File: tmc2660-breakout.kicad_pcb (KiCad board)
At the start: 2 copper layers, 26.9 x 31.1 mm, 18 parts, among them P1 SPI, P2 StepDir, P3 Motor, P4 VCC, P5 VMOT, U1 TMC2660

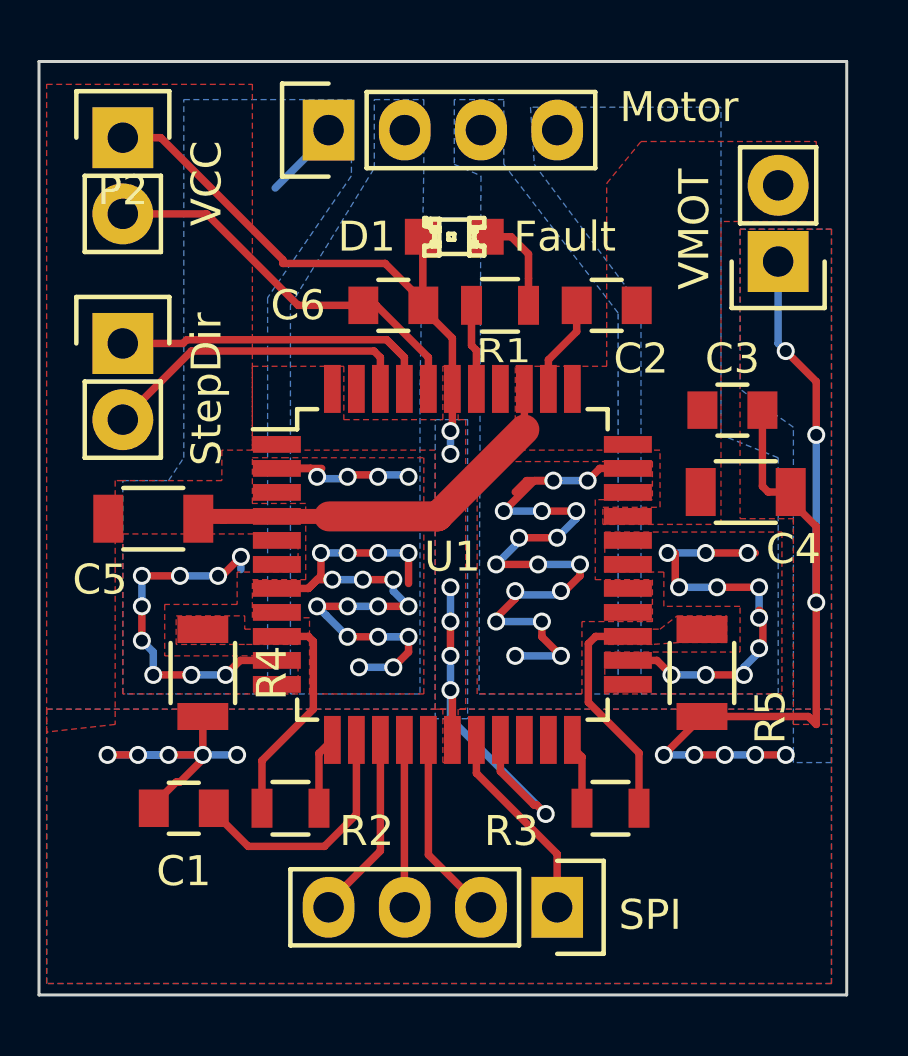
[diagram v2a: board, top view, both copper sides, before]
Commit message: o Add makefile to create fab files.
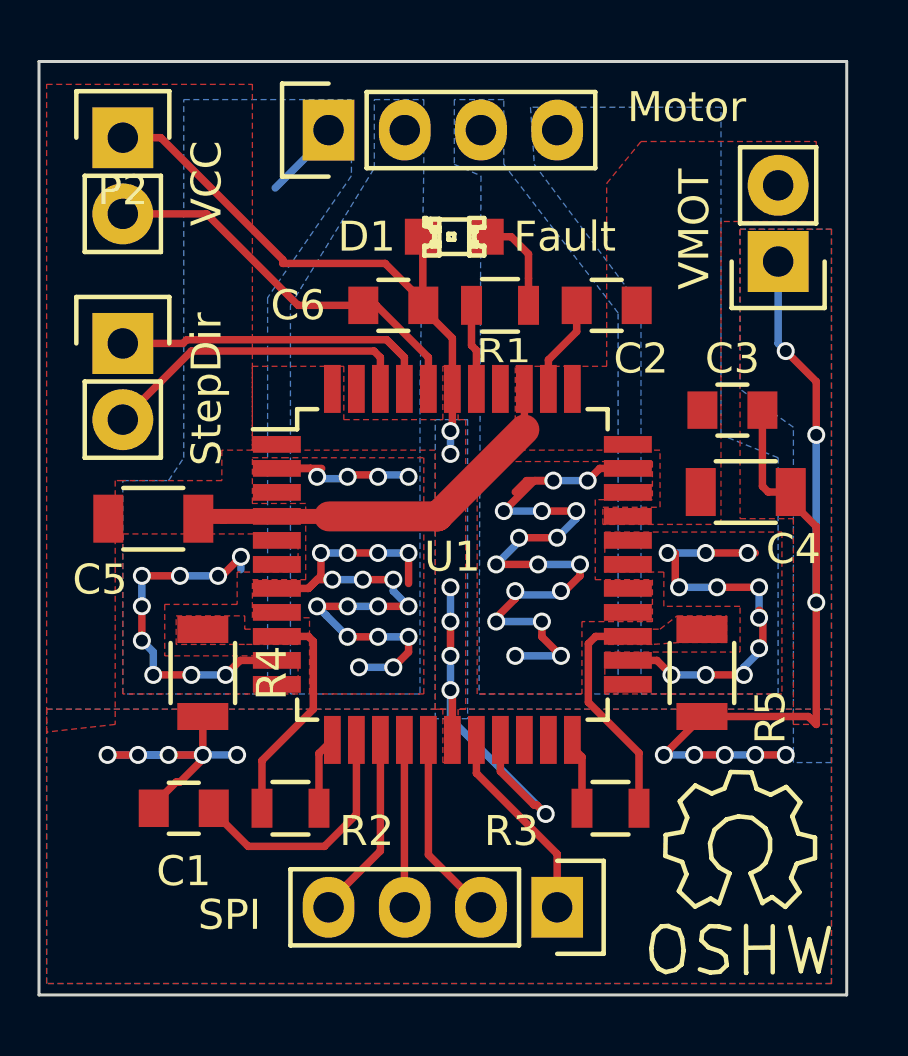
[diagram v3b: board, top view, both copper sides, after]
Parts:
- added REF**: Symbol_OSHW-Logo_SilkScreen, Symbols:Symbol_OSHW-Logo_SilkScreen, F.Cu at (139.4, 63.8)
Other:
- board text added: "%%gitversion%%"
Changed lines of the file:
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@@
 (kicad_pcb (version 4) (host pcbnew "(2015-12-17 BZR 6382, Git 22fdfa6)-product")
   (general
-    (links 56)
+    (links 0)
     (no_connects 0)
     (area 116.027999 37.541999 143.052001 68.757001)
     (thickness 1.6)
-    (drawings 5)
+    (drawings 6)
     (tracks 286)
     (zones 0)
-    (modules 18)
+    (modules 19)
     (nets 22)
   )
   (page A4)
   (layers
-    (0 F.Cu signal hide)
-    (31 B.Cu signal hide)
+    (0 F.Cu signal)
+    (31 B.Cu signal)
     (32 B.Adhes user)
     (33 F.Adhes user)
@@
       (effects (font (size 1 1) (thickness 0.15)))
     )
-    (fp_text value SPI (at 0.254 -3.1 360) (layer F.SilkS)
+    (fp_text value SPI (at 0.254 10.922 360) (layer F.SilkS)
       (effects (font (size 1 1) (thickness 0.15)))
     )
@@
       (effects (font (size 1 1) (thickness 0.15)))
     )
-    (fp_text value Motor (at 0.762 11.684 180) (layer F.SilkS)
+    (fp_text value Motor (at 0.762 11.938 180) (layer F.SilkS)
       (effects (font (size 1 1) (thickness 0.15)))
     )
@@
     )
   )
+  (module Symbols:Symbol_OSHW-Logo_SilkScreen locked (layer F.Cu)
+    (at 139.446 63.754)
+    (descr "Symbol, OSHW-Logo, Silk Screen,")
+    (tags "Symbol, OSHW-Logo, Silk Screen,")
+    (fp_text reference REF** (at 0.09906 -4.38912) (layer F.SilkS) hide
+      (effects (font (size 1 1) (thickness 0.15)))
+    )
+    (fp_text value Symbol_OSHW-Logo_SilkScreen (at 0.30988 6.56082) (layer F.Fab)
+      (effects (font (size 1 1) (thickness 0.15)))
+    )
+    (fp_line (start 1.66878 2.68986) (end 2.02946 4.16052) (layer F.SilkS) (width 0.15))
+    (fp_line (start 2.02946 4.16052) (end 2.30886 3.0988) (layer F.SilkS) (width 0.15))
+    (fp_line (start 2.30886 3.0988) (end 2.61874 4.17068) (layer F.SilkS) (width 0.15))
+    (fp_line (start 2.61874 4.17068) (end 2.9591 2.72034) (layer F.SilkS) (width 0.15))
+    (fp_line (start 0.24892 3.38074) (end 1.03886 3.37058) (layer F.SilkS) (width 0.15))
+    (fp_line (start 1.03886 3.37058) (end 1.04902 3.38074) (layer F.SilkS) (width 0.15))
+    (fp_line (start 1.04902 3.38074) (end 1.04902 3.37058) (layer F.SilkS) (width 0.15))
+    (fp_line (start 1.08966 2.65938) (end 1.08966 4.20116) (layer F.SilkS) (width 0.15))
+    (fp_line (start 0.20066 2.64922) (end 0.20066 4.21894) (layer F.SilkS) (width 0.15))
+    (fp_line (start 0.20066 4.21894) (end 0.21082 4.20878) (layer F.SilkS) (width 0.15))
+    (fp_line (start -0.35052 2.75082) (end -0.70104 2.66954) (layer F.SilkS) (width 0.15))
+    (fp_line (start -0.70104 2.66954) (end -1.02108 2.65938) (layer F.SilkS) (width 0.15))
+    (fp_line (start -1.02108 2.65938) (end -1.25984 2.86004) (layer F.SilkS) (width 0.15))
+    (fp_line (start -1.25984 2.86004) (end -1.29032 3.12928) (layer F.SilkS) (width 0.15))
+    (fp_line (start -1.29032 3.12928) (end -1.04902 3.37058) (layer F.SilkS) (width 0.15))
+    (fp_line (start -1.04902 3.37058) (end -0.6604 3.50012) (layer F.SilkS) (width 0.15))
+    (fp_line (start -0.6604 3.50012) (end -0.48006 3.66014) (layer F.SilkS) (width 0.15))
+    (fp_line (start -0.48006 3.66014) (end -0.43942 3.95986) (layer F.SilkS) (width 0.15))
+    (fp_line (start -0.43942 3.95986) (end -0.67056 4.18084) (layer F.SilkS) (width 0.15))
+    (fp_line (start -0.67056 4.18084) (end -0.9906 4.20878) (layer F.SilkS) (width 0.15))
+    (fp_line (start -0.9906 4.20878) (end -1.34112 4.09956) (layer F.SilkS) (width 0.15))
+    (fp_line (start -2.37998 2.64922) (end -2.6289 2.66954) (layer F.SilkS) (width 0.15))
+    (fp_line (start -2.6289 2.66954) (end -2.8702 2.91084) (layer F.SilkS) (width 0.15))
+    (fp_line (start -2.8702 2.91084) (end -2.9591 3.40106) (layer F.SilkS) (width 0.15))
+    (fp_line (start -2.9591 3.40106) (end -2.93116 3.74904) (layer F.SilkS) (width 0.15))
+    (fp_line (start -2.93116 3.74904) (end -2.7305 4.06908) (layer F.SilkS) (width 0.15))
+    (fp_line (start -2.7305 4.06908) (end -2.47904 4.191) (layer F.SilkS) (width 0.15))
+    (fp_line (start -2.47904 4.191) (end -2.16916 4.11988) (layer F.SilkS) (width 0.15))
+    (fp_line (start -2.16916 4.11988) (end -1.95072 3.93954) (layer F.SilkS) (width 0.15))
+    (fp_line (start -1.95072 3.93954) (end -1.8796 3.4798) (layer F.SilkS) (width 0.15))
+    (fp_line (start -1.8796 3.4798) (end -1.9304 3.07086) (layer F.SilkS) (width 0.15))
+    (fp_line (start -1.9304 3.07086) (end -2.03962 2.78892) (layer F.SilkS) (width 0.15))
+    (fp_line (start -2.03962 2.78892) (end -2.4003 2.65938) (layer F.SilkS) (width 0.15))
+    (fp_line (start -1.78054 0.92964) (end -2.03962 1.49098) (layer F.SilkS) (width 0.15))
+    (fp_line (start -2.03962 1.49098) (end -1.50114 2.00914) (layer F.SilkS) (width 0.15))
+    (fp_line (start -1.50114 2.00914) (end -0.98044 1.7399) (layer F.SilkS) (width 0.15))
+    (fp_line (start -0.98044 1.7399) (end -0.70104 1.89992) (layer F.SilkS) (width 0.15))
+    (fp_line (start 0.73914 1.8796) (end 1.06934 1.6891) (layer F.SilkS) (width 0.15))
+    (fp_line (start 1.06934 1.6891) (end 1.50876 2.0193) (layer F.SilkS) (width 0.15))
+    (fp_line (start 1.50876 2.0193) (end 1.9812 1.52908) (layer F.SilkS) (width 0.15))
+    (fp_line (start 1.9812 1.52908) (end 1.69926 1.04902) (layer F.SilkS) (width 0.15))
+    (fp_line (start 1.69926 1.04902) (end 1.88976 0.57912) (layer F.SilkS) (width 0.15))
+    (fp_line (start 1.88976 0.57912) (end 2.49936 0.39116) (layer F.SilkS) (width 0.15))
+    (fp_line (start 2.49936 0.39116) (end 2.49936 -0.28956) (layer F.SilkS) (width 0.15))
+    (fp_line (start 2.49936 -0.28956) (end 1.94056 -0.42926) (layer F.SilkS) (width 0.15))
+    (fp_line (start 1.94056 -0.42926) (end 1.7399 -1.00076) (layer F.SilkS) (width 0.15))
+    (fp_line (start 1.7399 -1.00076) (end 2.00914 -1.47066) (layer F.SilkS) (width 0.15))
+    (fp_line (start 2.00914 -1.47066) (end 1.53924 -1.9812) (layer F.SilkS) (width 0.15))
+    (fp_line (start 1.53924 -1.9812) (end 1.02108 -1.71958) (layer F.SilkS) (width 0.15))
+    (fp_line (start 1.02108 -1.71958) (end 0.55118 -1.92024) (layer F.SilkS) (width 0.15))
+    (fp_line (start 0.55118 -1.92024) (end 0.381 -2.46126) (layer F.SilkS) (width 0.15))
+    (fp_line (start 0.381 -2.46126) (end -0.30988 -2.47904) (layer F.SilkS) (width 0.15))
+    (fp_line (start -0.30988 -2.47904) (end -0.5207 -1.9304) (layer F.SilkS) (width 0.15))
+    (fp_line (start -0.5207 -1.9304) (end -0.9398 -1.76022) (layer F.SilkS) (width 0.15))
+    (fp_line (start -0.9398 -1.76022) (end -1.49098 -2.02946) (layer F.SilkS) (width 0.15))
+    (fp_line (start -1.49098 -2.02946) (end -2.00914 -1.50114) (layer F.SilkS) (width 0.15))
+    (fp_line (start -2.00914 -1.50114) (end -1.76022 -0.96012) (layer F.SilkS) (width 0.15))
+    (fp_line (start -1.76022 -0.96012) (end -1.9304 -0.48006) (layer F.SilkS) (width 0.15))
+    (fp_line (start -1.9304 -0.48006) (end -2.47904 -0.381) (layer F.SilkS) (width 0.15))
+    (fp_line (start -2.47904 -0.381) (end -2.4892 0.32004) (layer F.SilkS) (width 0.15))
+    (fp_line (start -2.4892 0.32004) (end -1.9304 0.5207) (layer F.SilkS) (width 0.15))
+    (fp_line (start -1.9304 0.5207) (end -1.7907 0.91948) (layer F.SilkS) (width 0.15))
+    (fp_line (start 0.35052 0.89916) (end 0.65024 0.7493) (layer F.SilkS) (width 0.15))
+    (fp_line (start 0.65024 0.7493) (end 0.8509 0.55118) (layer F.SilkS) (width 0.15))
+    (fp_line (start 0.8509 0.55118) (end 1.00076 0.14986) (layer F.SilkS) (width 0.15))
+    (fp_line (start 1.00076 0.14986) (end 1.00076 -0.24892) (layer F.SilkS) (width 0.15))
+    (fp_line (start 1.00076 -0.24892) (end 0.8509 -0.59944) (layer F.SilkS) (width 0.15))
+    (fp_line (start 0.8509 -0.59944) (end 0.39878 -0.94996) (layer F.SilkS) (width 0.15))
+    (fp_line (start 0.39878 -0.94996) (end -0.0508 -1.00076) (layer F.SilkS) (width 0.15))
+    (fp_line (start -0.0508 -1.00076) (end -0.44958 -0.89916) (layer F.SilkS) (width 0.15))
+    (fp_line (start -0.44958 -0.89916) (end -0.8509 -0.55118) (layer F.SilkS) (width 0.15))
+    (fp_line (start -0.8509 -0.55118) (end -1.00076 -0.09906) (layer F.SilkS) (width 0.15))
+    (fp_line (start -1.00076 -0.09906) (end -0.94996 0.39878) (layer F.SilkS) (width 0.15))
+    (fp_line (start -0.94996 0.39878) (end -0.70104 0.70104) (layer F.SilkS) (width 0.15))
+    (fp_line (start -0.70104 0.70104) (end -0.35052 0.89916) (layer F.SilkS) (width 0.15))
+    (fp_line (start -0.35052 0.89916) (end -0.70104 1.89992) (layer F.SilkS) (width 0.15))
+    (fp_line (start 0.35052 0.89916) (end 0.7493 1.89992) (layer F.SilkS) (width 0.15))
+  )
+  (gr_text %%gitversion%% (at 117.856 67.31 90) (layer B.SilkS)
+    (effects (font (size 1.5 1.5) (thickness 0.3)) (justify right mirror))
+  )
   (gr_text Fault (at 133.604 43.434) (layer F.SilkS)
